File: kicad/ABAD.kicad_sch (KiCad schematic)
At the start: 3 parts, among them U1 MS5611-01BA, U2 ESP32-WROOM-32, U3 MPU-6050

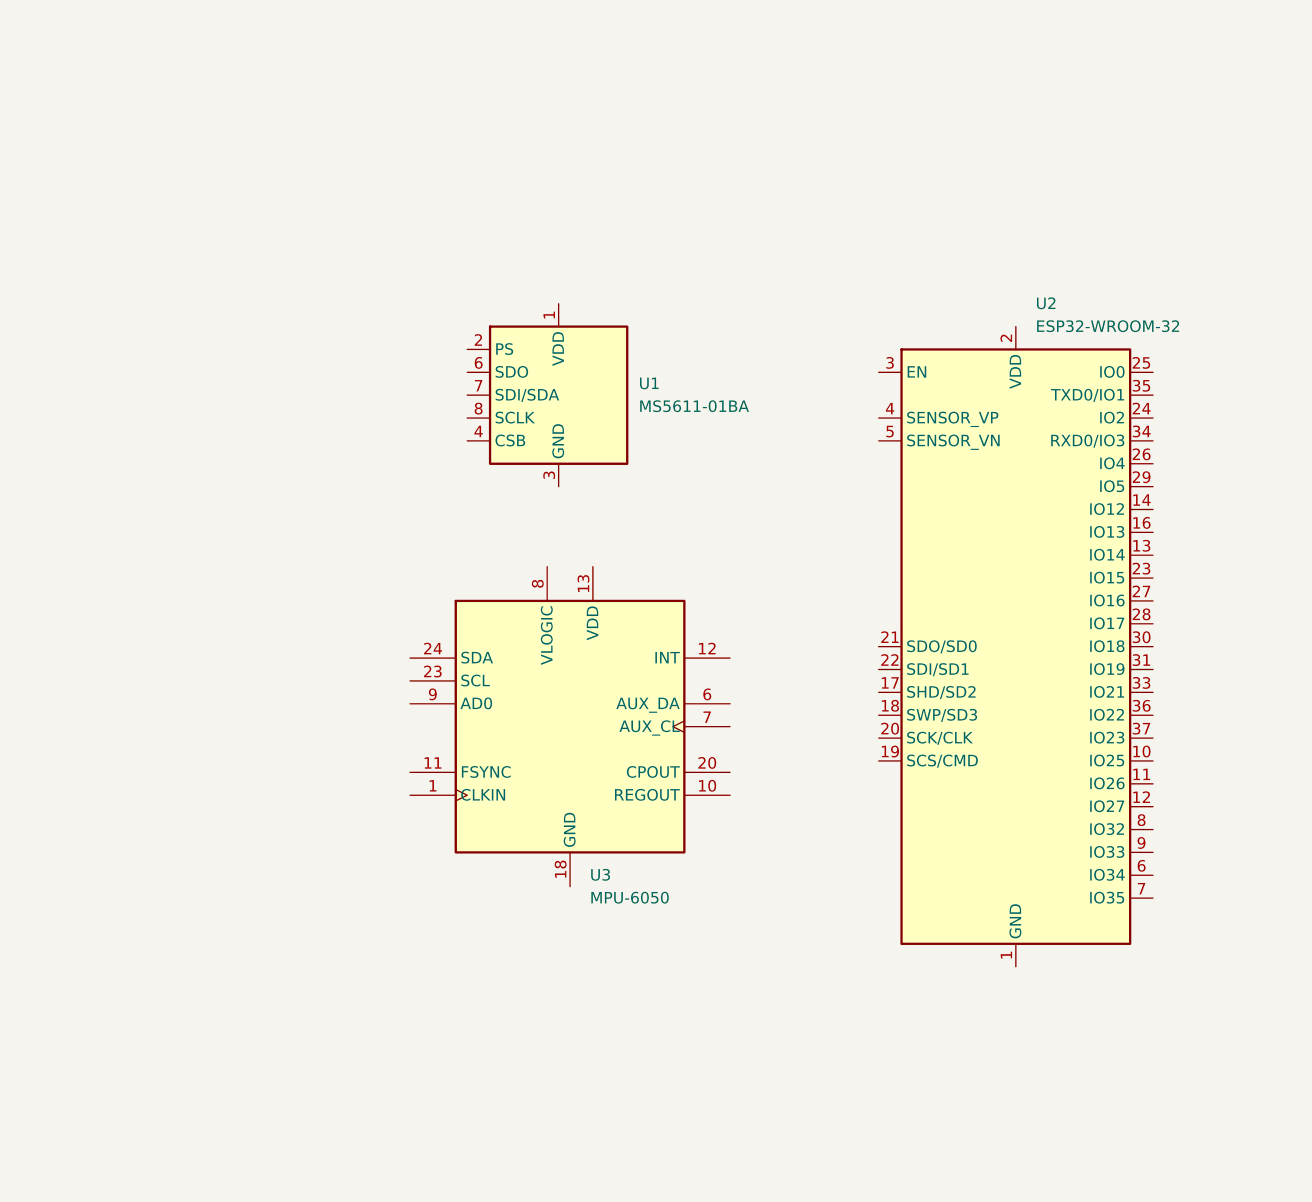
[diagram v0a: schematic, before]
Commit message: Schematic updated; pcb started; near completion
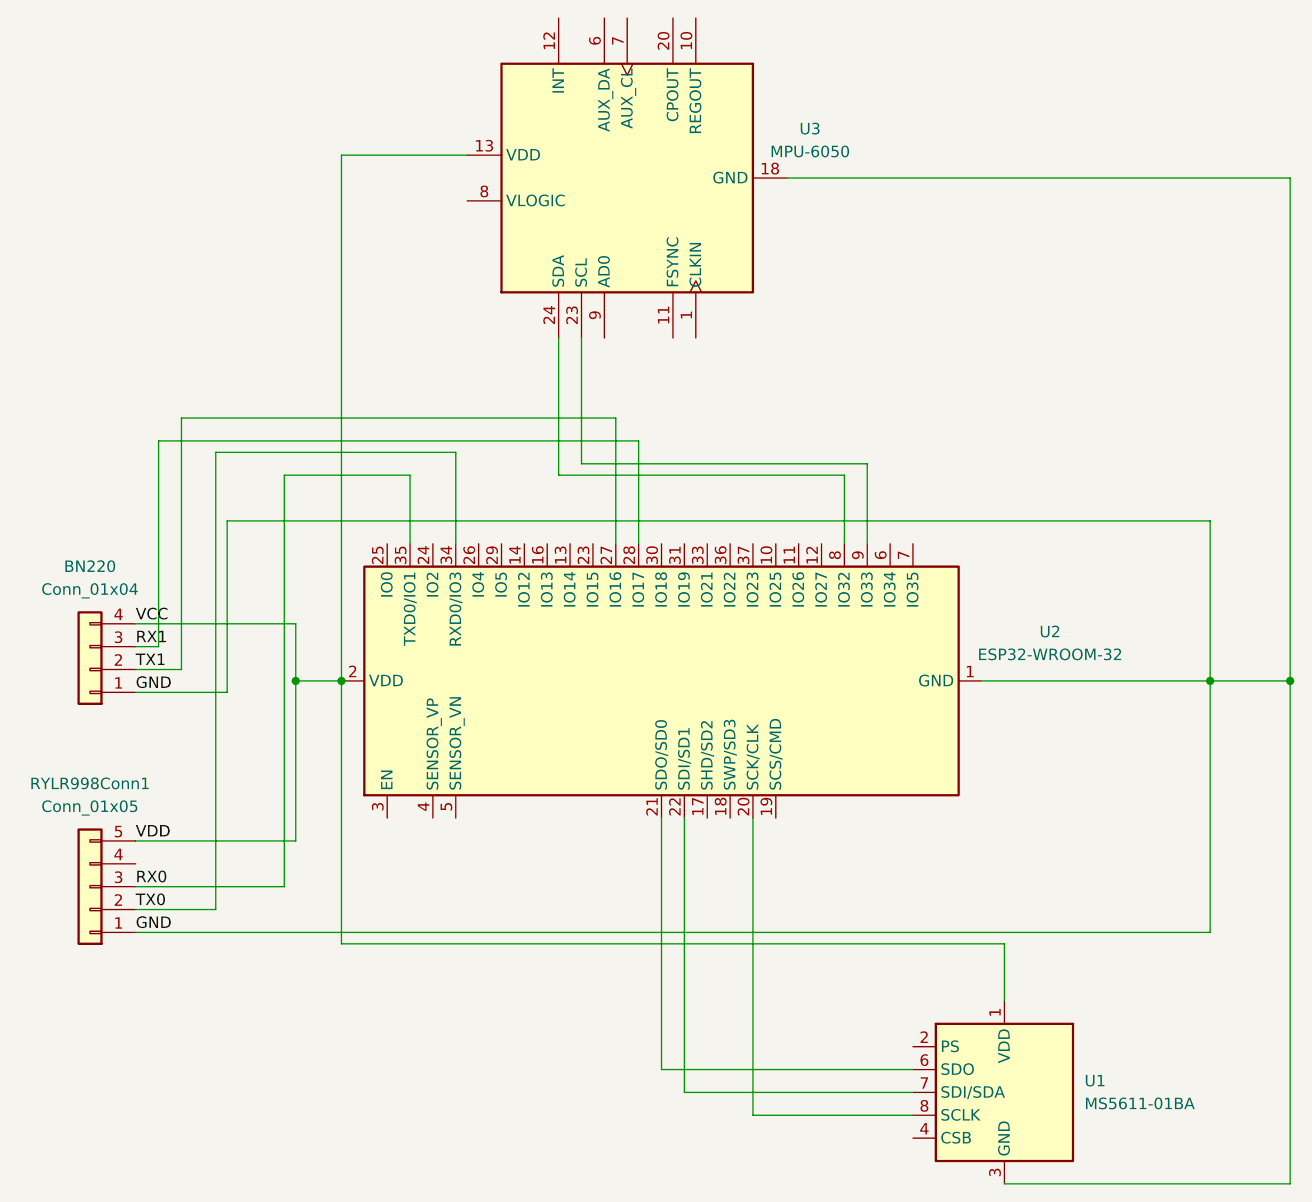
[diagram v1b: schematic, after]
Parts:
- added BN220: Conn_01x04, Connector_JST:JST_SH_BM04B-SRSS-TB_1x04-1MP_P1.00mm_Vertical, symbol Connector_Generic:Conn_01x04
- added RYLR998Conn1: Conn_01x05, Connector_PinSocket_1.00mm:PinSocket_1x05_P1.00mm_Vertical, symbol Connector_Generic:Conn_01x05
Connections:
- net VCC: now reaches U1.1 (VDD)
- net VCC: now also U2.2 (VDD), U3.13 (VDD), BN220.4 (Pin_4), RYLR998Conn1.5 (Pin_5)
- net GND: now reaches U1.3 (GND)
- net GND: now also U2.1 (GND), U2.15 (GND), U2.38 (GND), U2.39 (GND), U3.18 (GND), BN220.1 (Pin_1), RYLR998Conn1.1 (Pin_1)
- net at U1.6 (SDO): now also U2.21 (SDO/SD0)
- net at U1.7 (SDI/SDA): now also U2.22 (SDI/SD1)
- net at U1.8 (SCLK): now also U2.20 (SCK/CLK)
- net TX1: now reaches U2.27 (IO16)
- net TX1: now also BN220.2 (Pin_2)
- net RX1: now reaches U2.28 (IO17)
- net RX1: now also BN220.3 (Pin_3)
- net TX0: now reaches U2.34 (RXD0/IO3)
- net TX0: now also RYLR998Conn1.2 (Pin_2)
- net RX0: now reaches U2.35 (TXD0/IO1)
- net RX0: now also RYLR998Conn1.3 (Pin_3)
- net at U2.8 (IO32): now also U3.24 (SDA)
- net at U2.9 (IO33): now also U3.23 (SCL)
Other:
- moved on the sheet: U1, U2, U3

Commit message: Schematic_Jul12_Nile
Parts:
- removed BN220: Conn_01x04, Connector_JST:JST_SH_BM04B-SRSS-TB_1x04-1MP_P1.00mm_Vertical, symbol Connector_Generic:Conn_01x04
- removed RYLR998Conn1: Conn_01x05, Connector_PinSocket_1.00mm:PinSocket_1x05_P1.00mm_Vertical, symbol Connector_Generic:Conn_01x05
- removed U1: MS5611-01BA, Package_LGA:LGA-8_3x5mm_P1.25mm, symbol Sensor_Pressure:MS5611-01BA
- removed U2: ESP32-WROOM-32, RF_Module:ESP32-WROOM-32, symbol RF_Module:ESP32-WROOM-32
- added C1, C12: 100nF, Capacitor_SMD:C_0805_2012Metric, symbol Device:C_Small
- added C10, C11, C8, C9: 10uF, Capacitor_SMD:C_0805_2012Metric, symbol Device:C_Small
- added C13: 1uF, Capacitor_SMD:C_0805_2012Metric, symbol Device:C_Small
- added C14, C15, C7: 0.1uF, Capacitor_SMD:C_0805_2012Metric, symbol Device:C_Small
- added C2: 10nF, 4V, Capacitor_SMD:C_0805_2012Metric, symbol Device:C_Small
- added C3: 0.1uF, 4V, Capacitor_SMD:C_0805_2012Metric, symbol Device:C_Small
- added C4: 0.1uF, 2V, Capacitor_SMD:C_0805_2012Metric, symbol Device:C_Small
- added C5: 2.2nF, 50V, Capacitor_SMD:C_0805_2012Metric, symbol Device:C_Small
- added C6: 10uF 6.3V, Capacitor_SMD:C_0805_2012Metric, symbol Device:C_Small
- added D1: D_Schottky, Diode_SMD:D_3220_8050Metric, symbol Device:D_Schottky_Small
- added D2: GPS_LED_BLUE, LED_SMD:LED_0805_2012Metric, symbol Device:LED
- added D3: PWR_LED_RED, LED_SMD:LED_0805_2012Metric, symbol Device:LED
- added D4: RF_LED_GREEN, LED_SMD:LED_0805_2012Metric, symbol Device:LED
- added J1: USB_C_Receptacle_USB2.0_16P, Connector_USB:USB_Micro-B_Wuerth_629105150521_CircularHoles, symbol Connector:USB_C_Receptacle_USB2.0_16P
- added J2: BATT IO Screw Terminal, TerminalBlock_MetzConnect:TerminalBlock_MetzConnect_Type055_RT01502HDWU_1x02_P5.00mm_Horizontal, symbol Connector:Screw_Terminal_01x02
- added J3: Conn_Coaxial, Connector_Coaxial:SMA_Molex_73251-1153_EdgeMount_Horizontal, symbol Connector:Conn_Coaxial
- added L1: 1.5A 2.2uH, Inductor_SMD:L_0805_2012Metric, symbol Device:L
- added Q1, Q3: AO3401A, Package_TO_SOT_SMD:SOT-23, symbol Transistor_FET:AO3401A
- added R1, R2, R9: 10k, Resistor_SMD:R_0805_2012Metric, symbol Device:R_Small
- added R11, R12: 22Ω, Resistor_SMD:R_0805_2012Metric, symbol Device:R_Small
- added R3, R4: 5.1k, Resistor_SMD:R_0805_2012Metric, symbol Device:R_Small
- added R5: 100Ω, Resistor_SMD:R_0805_2012Metric, symbol Device:R_Small
- added R6, R7, R8: 68, Resistor_SMD:R_0805_2012Metric, symbol Device:R_Small
- added RESET_SW: SW_Push, symbol Switch:SW_Push
- added U1: ESP32-S3-WROOM-1, RF_Module:ESP32-S3-WROOM-1, symbol RF_Module:ESP32-S3-WROOM-1
- added U2: MS5611-01BA, Package_LGA:LGA-8_3x5mm_P1.25mm, symbol Sensor_Pressure:MS5611-01BA
- added U4: SAM-M8Q, RF_GPS:ublox_SAM-M8Q, symbol RF_GPS:SAM-M8Q
- added U5: USBLC6-2SC6, Package_TO_SOT_SMD:SOT-23-6, symbol Power_Protection:USBLC6-2SC6
- added U6: TPS63001, Package_SON:Texas_DRC0010J_ThermalVias, symbol Regulator_Switching:TPS63001
- added U7: ~, Lora1262_915TXCO:WIRELM-SMD_16P-L16.0-W16.0-P2.00_LORA-CC68-915MHZ-TCXO, symbol NiceRFLoRa1262_915:LORA1262-915TCXO
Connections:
- net VCC is gone; now on net +3.3V: U3.13 (VDD)
- net GND: now also U3.11 (FSYNC), U3.9 (AD0), C1.2, C10.2, C11.1, C12.1, C13.1, C14.2, C15.2, C2.1, C3.2, C4.2, C5.2, C6.2, C7.2, C8.2, C9.2, D2.1 (K), D3.1 (K), D4.1 (K), J1.A1 (GND), J1.A12 (GND), J1.B1 (GND), J1.B12 (GND), J1.S1 (SHIELD), J2.1 (Pin_1), J3.2 (Ext), Q3.1 (G), R3.2, R4.2, RESET_SW.2, U1.1 (GND), U1.40 (GND), U1.41 (GND), U2.3 (GND), U2.4 (CSB), U2.5 (CSB), U4.1 (GND), U4.10 (GND), U4.11 (GND), U4.15 (GND), U4.16 (GND), U4.20 (GND), U4.4 (GND), U4.5 (GND), U4.6 (GND), U5.2 (GND), U6.11 (PGND), U6.3 (PGND), U6.9 (GND), U7.1 (GND), U7.10 (GND), U7.8 (GND)
- net ACCEL_SDA: now reaches U3.24 (SDA)
- net ACCEL_SDA: now also U1.8 (IO15)
- net ACCEL_SCL: now reaches U3.23 (SCL)
- net ACCEL_SCL: now also U1.9 (IO16)
- net at U3.10 (REGOUT): now also C4.1
- net at U3.20 (CPOUT): now also C5.1
- net +3.3V: now reaches U3.8 (VLOGIC)
- net +3.3V: now also C1.1, C11.2, C12.2, C2.2, C3.1, C8.1, C9.1, R1.1, R2.1, R7.2, R9.2, U1.2 (3V3), U2.1 (VDD), U2.2 (PS), U4.17 (VCC), U4.2 (VCC_IO), U4.3 (V_BCKP), U6.1 (VOUT), U6.10 (FB), U7.13 (VCC)
- new net: J1.A5 (CC1), R4.1
- new net: D3.2 (A), R7.1
- new net: C7.1, R5.2, U6.6 (EN), U6.7 (PS/SYNC), U6.8 (VINA)
- new net: J3.1 (In), U7.9 (ANT)
- new net: L1.1, U6.4 (L1)
- new net: L1.2, U6.2 (L2)
- new net: D1.1 (K), Q1.2 (S), Q3.3 (D)
- new net: D2.2 (A), R6.1
- new net: J1.B5 (CC2), R3.1
- new net: D4.2 (A), R8.1
- new net +BATT: C10.1, C6.1, Q3.2 (S), R5.1, U6.5 (VIN)
- new net BARO_SCL: R2.2, U1.5 (IO5), U2.8 (SCLK)
- new net BARO_SDA: R1.2, U1.4 (IO4), U2.7 (SDI/SDA)
- new net BATT_RAW+: J2.2 (Pin_2), Q1.3 (D)
- new net BOOT: U1.27 (IO0)
- new net BUSY: U1.17 (IO9), U7.16 (BUSY)
- new net D+: C15.1, J1.A6 (D+), J1.B6 (D+), R11.1, R11.2, U1.14 (USB_D+), U5.1 (I/O1), U5.6 (I/O1)
- new net D-: C14.1, J1.A7 (D-), J1.B7 (D-), R12.1, R12.2, U1.13 (USB_D-), U5.3 (I/O2), U5.4 (I/O2)
- new net EN_RST: C13.2, R9.1, RESET_SW.1, U1.3 (EN)
- new net IO17: U1.10 (IO17), U4.14 (RXD)
- new net IO18: U1.11 (IO18), U4.13 (TXD)
- new net MISO: U1.21 (IO13), U7.2 (MISO)
- new net MOSI: U1.19 (IO11), U7.3 (MOSI)
- new net NRESET: U1.22 (IO14), U7.6 (NRESET)
- new net NSS: U1.18 (IO10), U7.5 (NSS)
- new net PPS: U1.6 (IO6), U4.7 (TIMEPULSE)
- new net PPS_LED: R6.2, U1.7 (IO7)
- new net RF_INT: U7.11 (DIO3)
- new net RF_LED: R8.2, U1.12 (IO8)
- new net SCLK: U1.20 (IO12), U7.4 (SCK)
- new net TXCO: U1.23 (IO21), U7.15 (DIO1)
- new net VBUS: D1.2 (A), J1.A4 (VBUS), J1.A9 (VBUS), J1.B4 (VBUS), J1.B9 (VBUS), Q1.1 (G), U5.5 (VBUS)
- no-connect marks 0 -> 15
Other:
- note added: "I/O"
- note added: "LORA1262-915TCXO"
- note added: "MICROCONTROLLER"
- note added: "POWER"
- note added: "Radio"
- note added: "SENSORS"

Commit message: schematic_Jul13_Nile
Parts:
- added C17: 22uF, Capacitor_SMD:C_0805_2012Metric, symbol Device:C_Small
- added C18, C8: 0.1uF, Capacitor_SMD:C_0805_2012Metric, symbol Device:C_Small
- added H1, H2, H3, H4: MountingHole, symbol Mechanical:MountingHole
- added R13, R14, R7: 10k, Resistor_SMD:R_0805_2012Metric, symbol Device:R_Small
- added RESET_SW2: SW_Push, symbol Switch:SW_Push
- added TP1: TXD0, symbol Connector:TestPoint
- added TP2: RXD0, symbol Connector:TestPoint
- added TP3: 3.3V, symbol Connector:TestPoint
- added TP4: VBUS, symbol Connector:TestPoint
- added TP5: BATT+, symbol Connector:TestPoint
- added TP6: BATT_RAW+, symbol Connector:TestPoint
- added TP7: GND, symbol Connector:TestPoint
- J1: renamed from J3; value Conn_Coaxial -> Edge mounted SMA
- J3: renamed from J2; value BATT IO Screw Terminal -> BATT Screw Terminal
- renumbered C12 to C1, C9 to C11, C2 to C12, C3 to C13, C1 to C14, C4 to C15, C5 to C16, C11 to C2, C6 to C3, C7 to C4, C15 to C5, C14 to C6, C13 to C7, C8 to C9, D4 to D2, D2 to D3, D3 to D4, J1 to J2, Q3 to Q2, R4 to R1, R7 to R10, R1 to R11, R2 to R12, R3 to R2, R5 to R3, R11 to R4, R12 to R5, R9 to R6, R6 to R9, RESET_SW to RESET_SW1, U7 to U1, U1 to U2, U5 to U3, U6 to U4, U4 to U5, U3 to U6, U2 to U7
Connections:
- net +3.3V: now also C17.2, C18.2, R13.1, R14.1, R7.2, TP3.1
- net +BATT: now also TP5.1
- net ACCEL_SCL: now also R14.2
- net ACCEL_SDA: now also R13.2
- net BATT_RAW+: now also TP6.1
- net BOOT: now also C8.2, R7.1, RESET_SW2.1
- net D+: no longer C5.1, R4.2, U3.6 (I/O1)
- net D-: no longer C6.1, R5.1, U3.4 (I/O2)
- net GND: now also C17.1, C18.1, C8.1, RESET_SW2.2, TP7.1
- net RF_INT: now also U2.25 (IO48)
- net VBUS: now also TP4.1
- net ACCEL_INT: now reaches U6.12 (INT)
- net ACCEL_INT: now also U2.24 (IO47)
- net RXD0: now reaches U2.36 (RXD0)
- net RXD0: now also TP2.1
- net TXD0: now reaches U2.37 (TXD0)
- net TXD0: now also TP1.1
- net IO17 renamed GPS_RX
- net IO18 renamed GPS_TX
- new net: C6.1, R5.1, U3.4 (I/O2)
- new net: C5.1, R4.2, U3.6 (I/O1)
- no-connect marks 15 -> 27
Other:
- note added: "LEDS"
- note added: "Not super needed"
- note added: "Pulled low for default addr"
- note added: "RADIO"
- note added: "TEST POINTS"
- note removed: "Radio"
- moved on the sheet: C5, C6, C7, J3, R1, R2, R4, R5, R6, RESET_SW1, U3

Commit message: schematic July 13 Nile
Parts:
- H1, H2, H3, H4: footprint (none) -> MountingHole:MountingHole_3.2mm_M3
- RESET_SW1, RESET_SW2: footprint (none) -> Button_Switch_THT:SW_PUSH_1P1T_6x3.5mm_H4.3_APEM_MJTP1243
- TP1, TP2, TP3, TP4, TP5, TP6, TP7: footprint (none) -> TestPoint:TestPoint_Pad_D1.0mm
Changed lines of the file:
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@@
 			)
 		)
-		(property "Footprint" ""
+		(property "Footprint" "TestPoint:TestPoint_Pad_D1.0mm"
 			(at 138.43 111.76 0)
 			(effects
@@
 			)
 		)
-		(property "Footprint" ""
+		(property "Footprint" "TestPoint:TestPoint_Pad_D1.0mm"
 			(at 163.83 101.6 0)
 			(effects
@@
 			)
 		)
-		(property "Footprint" ""
+		(property "Footprint" "TestPoint:TestPoint_Pad_D1.0mm"
 			(at 138.43 106.68 0)
 			(effects
@@
 			)
 		)
-		(property "Footprint" ""
+		(property "Footprint" "TestPoint:TestPoint_Pad_D1.0mm"
 			(at 138.43 96.52 0)
 			(effects
@@
 			)
 		)
-		(property "Footprint" ""
+		(property "Footprint" "TestPoint:TestPoint_Pad_D1.0mm"
 			(at 138.43 101.6 0)
 			(effects
@@
 			)
 		)
-		(property "Footprint" ""
+		(property "Footprint" "MountingHole:MountingHole_3.2mm_M3"
 			(at 200.66 107.95 0)
 			(effects
@@
 			)
 		)
-		(property "Footprint" ""
+		(property "Footprint" "MountingHole:MountingHole_3.2mm_M3"
 			(at 200.66 113.03 0)
 			(effects
@@
 			)
 		)
-		(property "Footprint" ""
+		(property "Footprint" "Button_Switch_THT:SW_PUSH_1P1T_6x3.5mm_H4.3_APEM_MJTP1243"
 			(at 149.86 176.53 0)
 			(effects
@@
 			)
 		)
-		(property "Footprint" ""
+		(property "Footprint" "Button_Switch_THT:SW_PUSH_1P1T_6x3.5mm_H4.3_APEM_MJTP1243"
 			(at 149.86 198.12 0)
 			(effects
@@
 			)
 		)
-		(property "Footprint" ""
+		(property "Footprint" "MountingHole:MountingHole_3.2mm_M3"
 			(at 200.66 97.79 0)
 			(effects
@@
 			)
 		)
-		(property "Footprint" ""
+		(property "Footprint" "TestPoint:TestPoint_Pad_D1.0mm"
 			(at 138.43 116.84 0)
 			(effects
@@
 			)
 		)
-		(property "Footprint" ""
+		(property "Footprint" "MountingHole:MountingHole_3.2mm_M3"
 			(at 200.66 102.87 0)
 			(effects
@@
 			)
 		)
-		(property "Footprint" ""
+		(property "Footprint" "TestPoint:TestPoint_Pad_D1.0mm"
 			(at 163.83 96.52 0)
 			(effects
